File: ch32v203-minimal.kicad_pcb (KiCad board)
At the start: 2 copper layers, 50 x 30 mm, 21 parts, among them J1 Conn_01x08, J3 Conn_01x04, J4 Conn_01x04, J5 Conn_02x10_Odd_Even, SW1 SW_Push, SW2 SW_Push, U1 AMS1117-3.3, U2 CH32V203K8T6, Y1 8MHz

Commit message: Add +5V connector
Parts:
- added J2: Conn_01x02_Pin, Connector_PinHeader_2.54mm:PinHeader_1x02_P2.54mm_Vertical, F.Cu at (138.3, 84.8)
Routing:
- net +5V: track 12.0 -> 15.1 mm
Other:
- board text added: "GND 5V"
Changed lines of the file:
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@@
+		)
+	)
+	(footprint "Connector_PinHeader_2.54mm:PinHeader_1x02_P2.54mm_Vertical"
+		(layer "F.Cu")
+		(at 138.305 84.805 -90)
+		(descr "Through hole straight pin header, 1x02, 2.54mm pitch, single row")
+		(tags "Through hole pin header THT 1x02 2.54mm single row")
+		(property "Reference" "J2"
+			(at 0 5.055 90)
+			(layer "F.SilkS")
+			(effects
+				(font
+					(size 1 1)
+					(thickness 0.15)
+				)
+			)
+		)
+		(property "Value" "Conn_01x02_Pin"
+			(at 0 4.92 90)
+			(layer "F.Fab")
+			(effects
+				(font
+					(size 1 1)
+					(thickness 0.15)
+				)
+			)
+		)
+		(property "Datasheet" ""
+			(at 0 0 90)
+			(layer "F.Fab")
+			(hide yes)
+			(effects
+				(font
+					(size 1.27 1.27)
+				)
+			)
+		)
+		(property "Description" "Generic connector, single row, 01x02, script generated"
+			(at 0 0 90)
+			(layer "F.Fab")
+			(hide yes)
+			(effects
+				(font
+					(size 1.27 1.27)
+				)
+			)
+		)
+		(property ki_fp_filters "Connector*:*_1x??_*")
+		(sheetname "/")
+		(sheetfile "ch32v203-minimal.kicad_sch")
+		(units
+			(unit
+				(name "A")
+				(pins "1" "2")
+			)
+		)
+		(attr through_hole)
+		(duplicate_pad_numbers_are_jumpers no)
+		(fp_line
+			(start -1.38 3.92)
+			(end 1.38 3.92)
+			(stroke
+				(width 0.12)
+				(type solid)
+			)
+			(layer "F.SilkS")
+		)
+		(fp_line
+			(start -1.38 1.27)
+			(end -1.38 3.92)
+			(stroke
+				(width 0.12)
+				(type solid)
+			)
+			(layer "F.SilkS")
+		)
+		(fp_line
+			(start -1.38 1.27)
+			(end 1.38 1.27)
+			(stroke
+				(width 0.12)
+				(type solid)
+			)
+			(layer "F.SilkS")
+		)
+		(fp_line
+			(start 1.38 1.27)
+			(end 1.38 3.92)
+			(stroke
+				(width 0.12)
+				(type solid)
+			)
+			(layer "F.SilkS")
+		)
+		(fp_line
+			(start -1.38 0)
+			(end -1.38 -1.38)
+			(stroke
+				(width 0.12)
+				(type solid)
+			)
+			(layer "F.SilkS")
+		)
+		(fp_line
+			(start -1.38 -1.38)
+			(end 0 -1.38)
+			(stroke
+				(width 0.12)
+				(type solid)
+			)
+			(layer "F.SilkS")
+		)
+		(fp_rect
+			(start -1.77 -1.77)
+			(end 1.77 4.32)
+			(stroke
+				(width 0.05)
+				(type solid)
+			)
+			(fill no)
+			(layer "F.CrtYd")
+		)
+		(fp_line
+			(start -1.27 3.81)
+			(end -1.27 -0.635)
+			(stroke
+				(width 0.1)
+				(type solid)
+			)
+			(layer "F.Fab")
+		)
+		(fp_line
+			(start 1.27 3.81)
+			(end -1.27 3.81)
+			(stroke
+				(width 0.1)
+				(type solid)
+			)
+			(layer "F.Fab")
+		)
+		(fp_line
+			(start -1.27 -0.635)
+			(end -0.635 -1.27)
+			(stroke
+				(width 0.1)
+				(type solid)
+			)
+			(layer "F.Fab")
+		)
+		(fp_line
+			(start -0.635 -1.27)
+			(end 1.27 -1.27)
+			(stroke
+				(width 0.1)
+				(type solid)
+			)
+			(layer "F.Fab")
+		)
+		(fp_line
+			(start 1.27 -1.27)
+			(end 1.27 3.81)
+			(stroke
+				(width 0.1)
+				(type solid)
+			)
+			(layer "F.Fab")
+		)
+		(fp_text user "${REFERENCE}"
+			(at 0 1.27 0)
+			(layer "F.Fab")
+			(effects
+				(font
+					(size 1 1)
+					(thickness 0.15)
+				)
+			)
+		)
+		(pad "1" thru_hole rect
+			(at 0 0 270)
+			(size 1.7 1.7)
+			(drill 1)
+			(layers "*.Cu" "*.Mask")
+			(remove_unused_layers no)
+			(net "+5V")
+			(pinfunction "Pin_1_1")
+			(pintype "passive")
+		)
+		(pad "2" thru_hole circle
+			(at 0 2.54 270)
+			(size 1.7 1.7)
+			(drill 1)
+			(layers "*.Cu" "*.Mask")
+			(remove_unused_layers no)
+			(net "GND")
+			(pinfunction "Pin_2_2")
+			(pintype "passive")
+		)
+		(embedded_fonts no)
+		(model "${KICAD10_3DMODEL_DIR}/Connector_PinHeader_2.54mm.3dshapes/PinHeader_1x02_P2.54mm_Vertical.step"
+			(offset
+				(xyz 0 0 0)
+			)
+			(scale
+				(xyz 1 1 1)
+			)
+			(rotate
+				(xyz 0 0 0)
+			)
 		)
 	)
@@
 		(layer "Edge.Cuts")
 	)
+	(gr_text "GND  5V"
+		(at 134 83.16 0)
+		(layer "F.SilkS")
+		(effects
+			(font
+				(size 0.8 0.8)
+				(thickness 0.08)
+			)
+			(justify left bottom)
+		)
+	)
 	(gr_text "3V3 DIO CLK GND"
 		(at 140.95 111.81 0)
@@
 	)
 	(gr_text "CH32V203 V1.0"
-		(at 132.9 85.41 0)
+		(at 140.45 85.41 0)
 		(layer "F.SilkS")
 		(effects
@@
 		(width 0.5)
 		(layer "F.Cu")
+		(net "+5V")
+	)
+	(segment
+		(start 139.2 87.5875)
+		(end 139.2 85.7)
+		(width 0.5)
+		(layer "F.Cu")
+		(net "+5V")
+	)
+	(segment
+		(start 139.2 85.7)
+		(end 138.305 84.805)
+		(width 0.5)
+		(layer "F.Cu")

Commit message: Add proto board
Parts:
- added D2: SS14, Diode_SMD:D_SMA, F.Cu at (135.1, 83.9)
- added H1: MountingHole_Pad, MountingHole:MountingHole_2.2mm_M2_DIN965_Pad, F.Cu at (133.7, 64.8)
- added H2: MountingHole_Pad, MountingHole:MountingHole_2.2mm_M2_DIN965_Pad, F.Cu at (178.7, 64.8)
- added H3: MountingHole_Pad, MountingHole:MountingHole_2.2mm_M2_DIN965_Pad, F.Cu at (133.7, 109.8)
- added H4: MountingHole_Pad, MountingHole:MountingHole_2.2mm_M2_DIN965_Pad, F.Cu at (178.7, 109.8)
- added H5: MountingHole_Pad, MountingHole:MountingHole_2.2mm_M2_DIN965_Pad, F.Cu at (149.8, 84.0)
- added TP1: TestPoint, 0_Local:Proto-1x16, F.Cu at (137.1, 76.5)
- added TP10: TestPoint, 0_Local:Proto-1x4, F.Cu at (154.9, 74.0)
- added TP11: TestPoint, 0_Local:Proto-1x4, F.Cu at (157.4, 74.0)
- added TP12: TestPoint, 0_Local:Proto-1x4, F.Cu at (160.0, 74.0)
- added TP13: TestPoint, 0_Local:Proto-1x4, F.Cu at (162.5, 74.0)
- added TP14: TestPoint, 0_Local:Proto-1x4, F.Cu at (165.0, 74.0)
- added TP15: TestPoint, 0_Local:Proto-1x4, F.Cu at (167.6, 74.0)
- added TP16: TestPoint, 0_Local:Proto-1x4, F.Cu at (170.1, 74.0)
- added TP17: TestPoint, 0_Local:Proto-1x4, F.Cu at (172.7, 74.0)
- added TP18: TestPoint, 0_Local:Proto-1x4, F.Cu at (175.2, 74.0)
- added TP2: TestPoint, 0_Local:Proto-1x16, F.Cu at (137.1, 79.1)
- added TP3: TestPoint, 0_Local:Proto-1x4, F.Cu at (137.1, 74.0)
- added TP4: TestPoint, 0_Local:Proto-1x4, F.Cu at (139.6, 74.0)
- added TP5: TestPoint, 0_Local:Proto-1x4, F.Cu at (142.2, 74.0)
- added TP6: TestPoint, 0_Local:Proto-1x4, F.Cu at (144.7, 74.0)
- added TP7: TestPoint, 0_Local:Proto-1x4, F.Cu at (147.2, 74.0)
- added TP8: TestPoint, 0_Local:Proto-1x4, F.Cu at (149.8, 74.0)
- added TP9: TestPoint, 0_Local:Proto-1x4, F.Cu at (152.3, 74.0)
- moved J2 5.69 mm to (144.0, 84.5)
- moved C8 3.18 mm to (176.4, 104.9)
- moved J1 1.91 mm to (134.3, 87.6)
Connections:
- C1 pad 1: +5V -> VBUS
- J1 pad 2: +5V -> /+5V
- J2 pad 1: +5V -> VBUS
- U1 pad 3: +5V -> VBUS
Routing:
- net GND: track 24.7 -> 84.0 mm, vias 57 -> 51
- net +3V3: track 0.02 -> 54.3 mm
- net +5V: track 15.1 -> 0.00 mm
- net VBUS: track 0.00 -> 12.4 mm
- net Row 9: track 0.00 -> 7.62 mm
- net Row 8: track 0.00 -> 7.62 mm
- net Row 7: track 0.00 -> 7.62 mm
- net Row 6: track 0.00 -> 7.62 mm
- net Row 5: track 0.00 -> 7.62 mm
- net Row 4: track 0.00 -> 7.62 mm
- net Row 3: track 0.00 -> 7.62 mm
- net Row 2: track 0.00 -> 7.62 mm
- net Row 16: track 0.00 -> 7.62 mm
- net Row 15: track 0.00 -> 7.62 mm
- net Row 14: track 0.00 -> 7.62 mm
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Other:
- board size 50 x 30 mm -> 50 x 50 mm
- board text added: "CH32V203 Proto Board"
- board text added: "Gnd Vbus"
- board text removed: "CH32V203 V1.0"
- board text removed: "GND 5V"

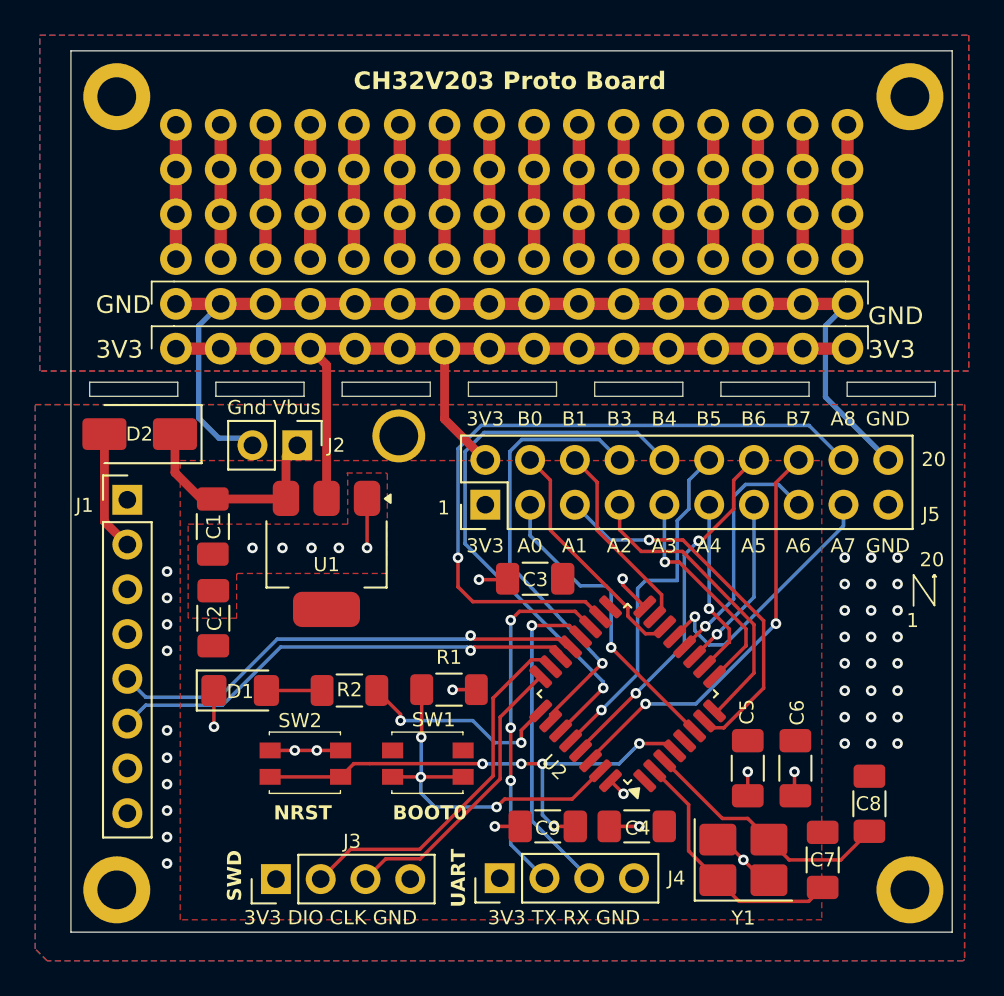
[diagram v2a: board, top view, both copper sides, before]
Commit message: Swap LDO for MCP1700
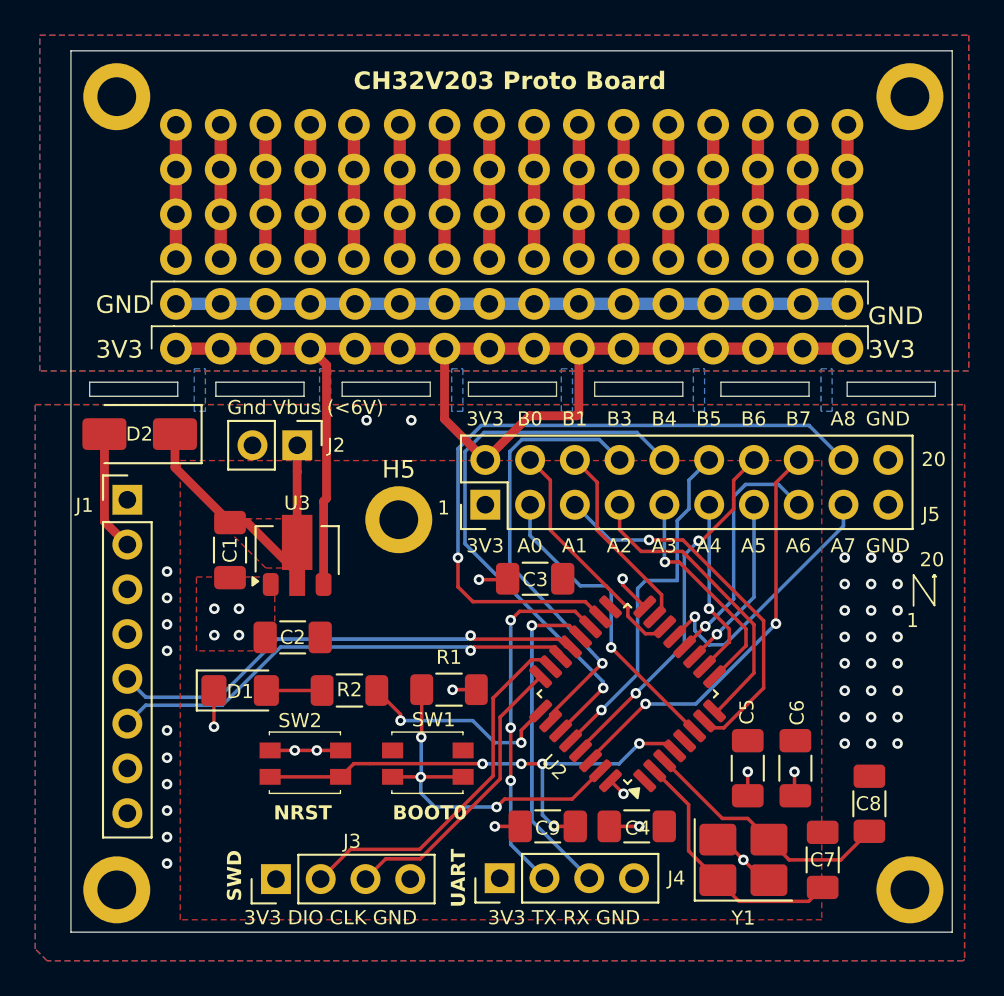
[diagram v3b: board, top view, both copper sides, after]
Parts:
- removed U1: AMS1117-3.3, Package_TO_SOT_SMD:SOT-223-3_TabPin2
- added U3: MCP1700x-330xxMB, Package_TO_SOT_SMD:SOT-89-3, F.Cu at (144.0, 90.5)
- C1: value 10uF -> 1uF
- C2: value 22uF -> 4.7uF
- moved H5 4.75 mm to (149.7, 88.8)
- moved C2 4.64 mm to (143.7, 95.4), turned to 180 degrees
- moved C1 1.65 mm to (140.2, 90.5)
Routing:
- net GND: track 84.0 -> 59.9 mm, vias 51 -> 52
- net +3V3: track 54.3 -> 69.3 mm
- net VBUS: track 12.4 -> 20.2 mm
- added copper zone on F.Cu, net VBUS
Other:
- board text added: "Gnd Vbus (<6V)"
- board text removed: "Gnd Vbus"

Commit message: Add battery-charging circuit
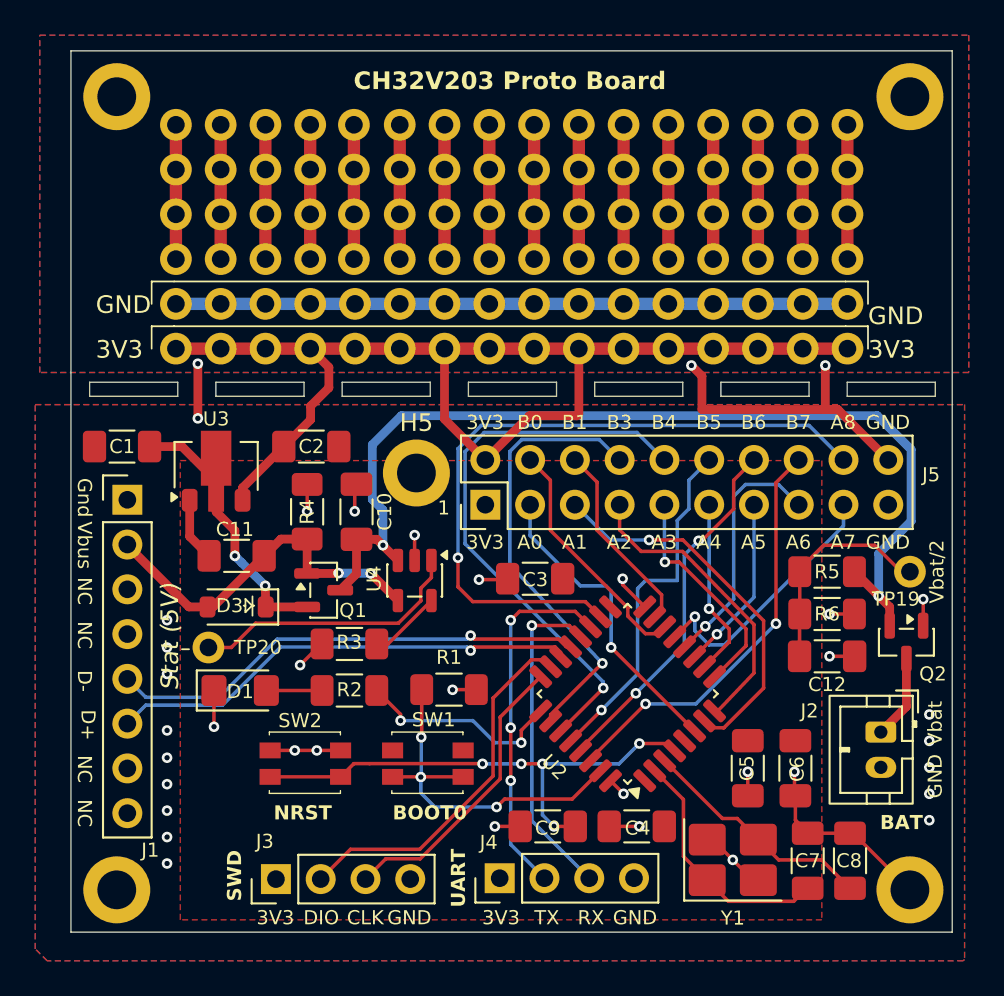
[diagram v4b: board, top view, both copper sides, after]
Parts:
- removed D2: SS14, Diode_SMD:D_SMA
- added C10: 4.7uF, Capacitor_SMD:C_1206_3216Metric_Pad1.33x1.80mm_HandSolder, F.Cu at (147.3, 88.3)
- added C11: 4.7uF, Capacitor_SMD:C_1206_3216Metric_Pad1.33x1.80mm_HandSolder, F.Cu at (140.6, 90.8)
- added C12: 100nF, Capacitor_SMD:C_1206_3216Metric_Pad1.33x1.80mm_HandSolder, F.Cu at (174.1, 96.5)
- added D3: B5819W SL, Diode_SMD:D_SOD-123, F.Cu at (140.6, 93.7)
- added Q1: AO3401A, Package_TO_SOT_SMD:SOT-23, F.Cu at (145.5, 92.8)
- added Q2: AO3401A, Package_TO_SOT_SMD:SOT-23, F.Cu at (178.6, 95.7)
- added R3: 4K7, Resistor_SMD:R_1206_3216Metric_Pad1.30x1.75mm_HandSolder, F.Cu at (146.9, 95.8)
- added R4: 10K, Resistor_SMD:R_1206_3216Metric_Pad1.30x1.75mm_HandSolder, F.Cu at (144.6, 88.3)
- added R5: 1M, Resistor_SMD:R_1206_3216Metric_Pad1.30x1.75mm_HandSolder, F.Cu at (174.1, 91.7)
- added R6: 1M, Resistor_SMD:R_1206_3216Metric_Pad1.30x1.75mm_HandSolder, F.Cu at (174.1, 94.1)
- added TP19: Vbat/2, 0_Local:TP-PlatedHole, F.Cu at (178.8, 91.7)
- added TP20: Chg Stat, 0_Local:TP-PlatedHole, F.Cu at (138.9, 96.0)
- added U4: MCP73831-2-OT, Package_TO_SOT_SMD:SOT-23-5, F.Cu at (150.7, 92.2)
- C1: value 1uF -> 10uF
- J2: footprint Connector_PinHeader_2.54mm:PinHeader_1x02_P2.54mm_Vertical -> Connector_JST:JST_PH_B2B-PH-K_1x02_P2.00mm_Vertical
- moved J2 36.9 mm to (177.1, 100.8)
- moved C2 10.9 mm to (144.8, 84.6), turned to 0 degrees
- moved C1 8.49 mm to (134.1, 84.6), turned to 180 degrees
- moved U3 6.63 mm to (139.4, 85.7)
- moved C8 3.42 mm to (175.3, 108.1)
- moved H5 2.83 mm to (150.8, 86.1)
- moved C7 0.85 mm to (172.9, 108.1)
- moved Y1 0.60 mm to (168.7, 108.1)
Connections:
- C1 pad 1: VBUS -> /Vsys
- J1 pad 2: /+5V -> /Vbus
- J2 pad 1: VBUS -> /Vbat
- U3 pad 2: VBUS -> /Vsys
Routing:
- net /Vbat (P): track 0.00 -> 57.1 mm, vias 0 -> 2
- net GND: track 59.9 -> 104.4 mm, vias 52 -> 37
- net /Vbus: track 0.00 -> 20.6 mm, vias 0 -> 2
- net VBUS: track 20.2 -> 0.00 mm
- net Net-(U4-STAT): track 0.00 -> 15.7 mm
- net /Vsys: track 0.00 -> 15.3 mm, vias 0 -> 2
- net Net-(C12-Pad1): track 0.00 -> 12.4 mm
- net /+5V: track 6.80 -> 0.00 mm
- net /Vbat: track 0.00 -> 4.76 mm
- net Net-(U4-PROG): track 0.00 -> 4.12 mm
- net +3V3: track 69.3 -> 66.6 mm
- net Net-(U2-OSC_OUT/PD1): track 14.6 -> 13.5 mm
- removed copper zone on F.Cu, net VBUS
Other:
- board text added: "BAT"
- board text added: "CLK"
- board text added: "D+"
- board text added: "D-"
- board text added: "DIO"
- board text added: "Gnd"
- board text added: "NC"
- board text added: "RX"
- board text added: "Stat (5V)"
- board text added: "TX"
- board text added: "Vbat"
- board text added: "Vbat/2"
- board text added: "Vbus"
- board text removed: "3V3 DIO CLK GND"
- board text removed: "3V3 TX RX GND"
- board text removed: "Gnd Vbus (<6V)"

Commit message: Add USB protection + misc fixes
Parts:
- added D2: SMF5V0A, Diode_SMD:D_SMF, F.Cu at (138.1, 107.3)
- added JP1: Jumper_2_Open, Jumper:SolderJumper-2_P1.3mm_Open_TrianglePad1.0x1.5mm, F.Cu at (171.2, 99.0)
- added JP2: Jumper_2_Open, Jumper:SolderJumper-2_P1.3mm_Open_TrianglePad1.0x1.5mm, F.Cu at (153.8, 92.6)
- added R7: 5K1, Resistor_SMD:R_1206_3216Metric_Pad1.30x1.75mm_HandSolder, F.Cu at (132.9, 91.5)
- added R8: 5K1, Resistor_SMD:R_1206_3216Metric_Pad1.30x1.75mm_HandSolder, F.Cu at (135.6, 91.5)
- added U1: USBLC6-2SC6, Package_TO_SOT_SMD:SOT-23-6, F.Cu at (142.6, 99.3)
- C7, C8: value 20pF -> 12pF
- J1: value Conn_01x08 -> USB_C_Receptacle_USB2.0_16P; footprint Connector_PinHeader_2.54mm:PinHeader_1x08_P2.54mm_Vertical -> Connector_USB:USB_C_Receptacle_HRO_TYPE-C-31-M-12
- TP19, TP20: footprint 0_Local:TP-PlatedHole -> TestPoint:TestPoint_Pad_1.0x1.0mm
- moved J1 13.2 mm to (135.3, 100.8), turned to -90 degrees
- moved TP20 12.9 mm to (151.8, 95.9)
- moved D1 6.69 mm to (146.9, 101.0), turned to 180 degrees
- moved SW1 2.72 mm to (149.4, 104.0), turned to 180 degrees
- moved SW2 1.66 mm to (143.7, 104.0), turned to 180 degrees
- moved C3 0.15 mm to (157.6, 92.1)
- moved TP19 0.07 mm to (178.8, 91.8)
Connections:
- net Net-(U2-OSC_IN/PD0) renamed /OSC_IN
- net Net-(U2-OSC_OUT/PD1) renamed /OSC_OUT
- U2 pad 21: /D- -> D-
- U2 pad 22: /D+ -> D+
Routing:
- net +3V3: track 66.6 -> 149.5 mm, vias 0 -> 2
- net /D-: track 27.3 -> 0.00 mm, vias 1 -> 0
- net /D+: track 26.9 -> 0.00 mm, vias 1 -> 0
- net GND: track 104.4 -> 78.9 mm, vias 37 -> 40
- net D-: track 0.00 -> 20.4 mm, vias 0 -> 2
- net D+: track 0.00 -> 17.6 mm, vias 0 -> 2
- net /Vbus: track 20.6 -> 38.0 mm, vias 2 -> 4
- net PB1: track 11.1 -> 25.8 mm, vias 0 -> 2
- net Net-(J1-CC2): track 0.00 -> 13.3 mm
- net Net-(JP2-B): track 15.7 -> 6.82 mm
- net Net-(J1-CC1): track 0.00 -> 8.53 mm
- net Net-(J1-D+-PadA6): track 0.00 -> 7.20 mm
- net Net-(J1-D--PadA7): track 0.00 -> 6.57 mm
- net PB3: track 25.6 -> 28.4 mm, vias 1 -> 2
- net Net-(JP1-B): track 12.4 -> 15.1 mm
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- removed copper zone on F.Cu, net +3V3
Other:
- board text added: "CH32V203 Proto Board V1.1 https://github.com/paulc/ch32v203-minimal"
- board text added: "Chg"
- board text added: "JP1: Vbat/2 -> PB1 JP2: Battery Status -> PB0"
- board text removed: "D+"
- board text removed: "D-"
- board text removed: "Gnd"
- board text removed: "NC"
- board text removed: "NRST"
- board text removed: "Stat (5V)"
- board text removed: "Vbus"

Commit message: Update production files
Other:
- board text added: "CH32V203 Proto Board V1.1"
- board text added: "JP1: Vbat/2 -> PB1 (ADC9) JP2: Battery Status -> PB3 (FT)"
- board text added: "https://github.com/paulc/ch32v203-minimal"
- board text removed: "CH32V203 Proto Board V1.1 https://github.com/paulc/ch32v203-minimal"
- board text removed: "JP1: Vbat/2 -> PB1 JP2: Battery Status -> PB0"
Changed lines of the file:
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@@
 		)
 	)
-	(gr_text "JP1: Vbat/2 -> PB1\nJP2: Battery Status -> PB0"
+	(gr_text "JP1: Vbat/2 -> PB1 (ADC9)\nJP2: Battery Status -> PB3 (FT)"
 		(at 160.75 106.06 0)
 		(layer "B.SilkS")
@@
 		)
 	)
-	(gr_text "CH32V203 Proto Board V1.1\nhttps://github.com/paulc/ch32v203-minimal"
-		(at 160.65 94.66 0)
+	(gr_text "https://github.com/paulc/ch32v203-minimal"
+		(at 160.65 95.01 0)
 		(layer "B.SilkS")
 		(effects
@@
 		)
 	)
+	(gr_text "CH32V203 Proto Board V1.1"
+		(at 160.55 93.11 0)
+		(layer "B.SilkS")
+		(effects
+			(font
+				(size 1 1)
+				(thickness 0.2)
+				(bold yes)
+			)
+			(justify left bottom mirror)
+		)
+	)
